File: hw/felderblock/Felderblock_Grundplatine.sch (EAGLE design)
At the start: 54 parts, among them IC2 LM2936, IC3 ULN2803, IC4 MCP2300X/P, J1 RJ11, J2 RJ11, M1 ARDUINO-NANO-3.0, T2 BC337, X1 TASTENSPERRE1, X2 TASTENSPERRE2, X3 SCHL-SPERRE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

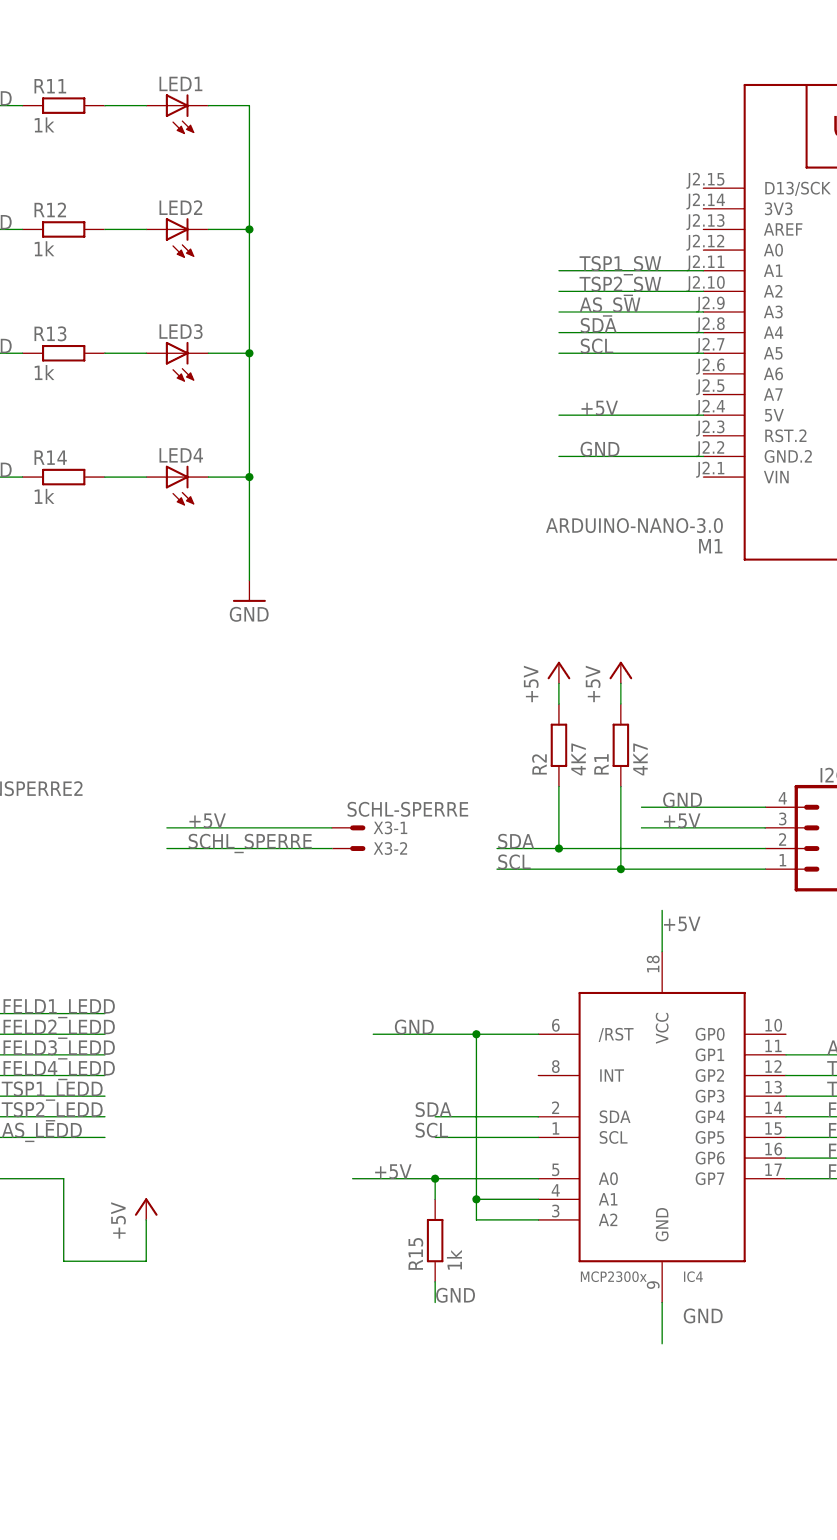
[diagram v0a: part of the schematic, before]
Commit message: corrected errors
LEDs connections corrected, address for MCP23008 corrected, reset for MCP23008 corrected
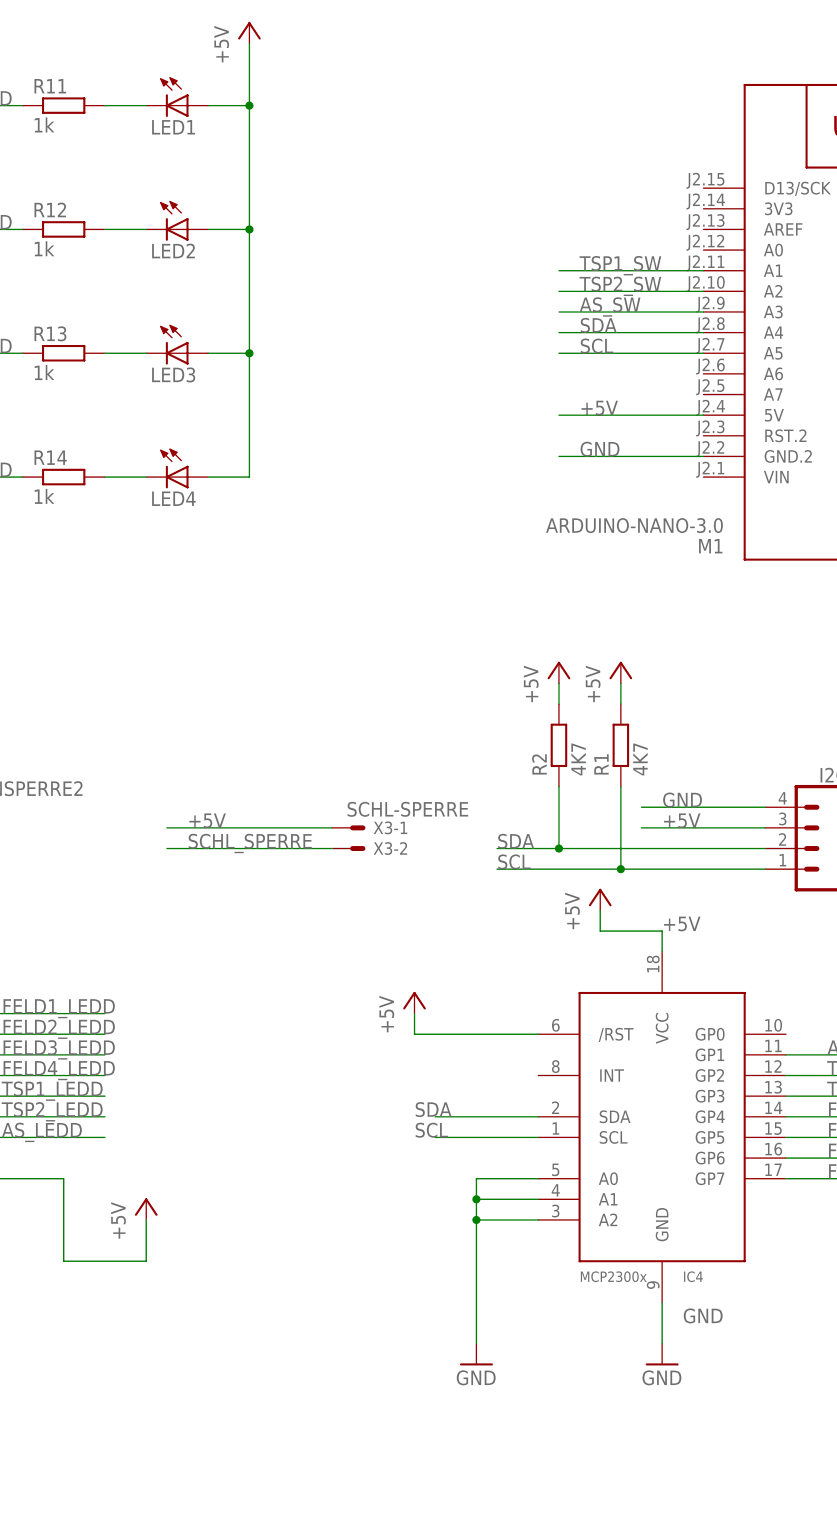
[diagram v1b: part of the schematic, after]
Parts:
- removed R15: 1k, resistor:R-EU_0207/7
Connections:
- removed net N$5: LED2.A, R12.2
- removed net N$8: LED3.A, R13.2
- removed net N$9: LED4.A, R14.2
- new net N$1: LED1.C, R11.2
- new net N$2: LED2.C, R12.2
- new net N$3: LED3.C, R13.2
- net +5V: now also IC4./RST, LED1.A, LED2.A, LED3.A, LED4.A; no longer IC4.A0, R15.2
- net GND: now also IC4.A0; no longer IC4./RST, LED1.C, LED2.C, LED3.C, LED4.C, R15.1
- net N$4: now also LED4.C, R14.2; no longer LED1.A, R11.2
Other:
- moved on the sheet: LED1, LED2, LED3, LED4

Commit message: Changed to PCA9685
- Changed LED-driver to PCA9685
- Now two LED per field
- Use LN-circuit with comparator
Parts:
- removed C2, C3: 100nF, resistor:C-EU025-025X050
- removed C6: 47pF, resistor:C-EU025-024X044
- removed C7: 1nF, resistor:C-EU025-025X050
- removed IC3: ULN2803, uln-udn:ULN2803ADIL18
- removed IC4: MCP2300X/P, adafruit:MCP2300X/P
- removed R11, R12, R13, R14: 1k, resistor:R-EU_0207/7
- added IC1: LM311N, linear:LM311N
- added LED5, LED6, LED7, LED8: (no value), led:LED3MM
- added R3: 4.7k, resistor:R-EU_0207/7
- added U$1: ADA9685-STACK, ada9685:ADA9685-STACK
- LED1, LED2, LED3, LED4: device led:LED10MM -> led:LED3MM
- R16: value 12R -> 47k
- R17: value 12R -> 150k
- R18: value 130K -> 10k
- R19: value 47k -> 22k
- R20: value 3K3 -> 220k
- X3: device con-molex:22-23-2021 -> con-molex:22-23-2041
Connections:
- removed net AS_LEDD: IC3.O7, X5-3.S
- removed net FELD1_LED: IC3.I1, IC4.GP7
- removed net FELD1_LEDD: IC3.O1, R11.1
- removed net FELD2_LED: IC3.I2, IC4.GP6
- removed net FELD2_LEDD: IC3.O2, R12.1
- removed net FELD3_LED: IC3.I3, IC4.GP5
- removed net FELD3_LEDD: IC3.O3, R13.1
- removed net FELD4_LED: IC3.I4, IC4.GP4
- removed net FELD4_LEDD: IC3.O4, R14.1
- removed net LN_INTERN: R17.2, R18.2, T2.C
- removed net N$1: LED1.C, R11.2
- removed net N$11: C6.1, R16.2, R17.1
- removed net N$2: LED2.C, R12.2
- removed net N$3: LED3.C, R13.2
- removed net N$4: LED4.C, R14.2
- removed net SCHL_SPERRE: M1.D2, X3-2.S
- removed net TSP1_LEDD: IC3.O5, X1-3.S
- removed net TSP2_LEDD: IC3.O6, X2-3.S
- new net FELD1_LED_RD: LED1.C, U$1.PWM0
- new net FELD1_LED_WS: LED5.C, U$1.PWM4
- new net FELD2_LED_RD: LED2.C, U$1.PWM1
- new net FELD2_LED_WS: LED6.C, U$1.PWM5
- new net FELD3_LED_RD: LED3.C, U$1.PWM2
- new net FELD3_LED_WS: LED7.C, U$1.PWM6
- new net FELD4_LED_RD: LED4.C, U$1.PWM3
- new net FELD4_LED_WS: LED8.C, U$1.PWM7
- new net N$5: IC1.+IN, R16.1, R17.2, R20.2
- new net N$8: IC1.-IN, R18.1, R19.2
- new net SCHL_SP_LED: U$1.PWM14, X3-3.S
- new net SCHL_SP_SW: M1.A2, X3-4.S
- net +5V: now also IC1.V+, LED5.A, LED6.A, LED7.A, LED8.A, R18.2, U$1.V+, U$1.VCC, X3-2.S; no longer C2.1, C3.1, IC3.CD+, IC4./RST, IC4.VCC, X3-1.S
- net AS_LED: now also U$1.PWM15, X5-3.S; no longer IC3.I7, IC4.GP1
- net BASE: now also R3.2; no longer C7.2, R20.2
- net GND: now also IC1.GND, IC1.V-, R17.1, U$1.GND, X3-1.S; no longer C2.2, C3.2, C6.2, IC3.GND, IC4.A0, IC4.A1, IC4.A2, IC4.GND
- net LN_RX: now also IC1.OUT, R20.1; no longer R18.1, R19.2
- net LN_TX: now also R3.1; no longer C7.1, R20.1
- net LOCONET: now also R16.2, T2.C; no longer R16.1
- net MI_FWD: now also M1.D2; no longer M1.D6
- net MI_REV: now also M1.D3; no longer M1.D5
- net SCL: now also U$1.SCL; no longer IC4.SCL
- net SDA: now also U$1.SDA; no longer IC4.SDA
- net TSP1_LED: now also U$1.PWM12, X1-3.S; no longer IC3.I5, IC4.GP3
- net TSP1_SW: now also M1.A0; no longer M1.A1
- net TSP2_LED: now also U$1.PWM13, X2-3.S; no longer IC3.I6, IC4.GP2
- net TSP2_SW: now also M1.A1; no longer M1.A2
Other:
- moved on the sheet: I2C, LED1, LED2, LED3, LED4, M1, R1, R10, R16, R17, R18, R19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

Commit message: Rearranged order of LED and switches
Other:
- moved on the sheet: U$1
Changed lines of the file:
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@@
 <?xml version="1.0" encoding="utf-8"?>
 <!DOCTYPE eagle SYSTEM "eagle.dtd">
-<eagle version="7.7.0">
+<eagle version="7.3.0">
 <drawing>
 <settings>
@@
 <grid distance="0.1" unitdist="inch" unit="inch" style="lines" multiple="1" display="no" altdistance="0.01" altunitdist="inch" altunit="inch"/>
 <layers>
-<layer number="1" name="Top" color="4" fill="1" visible="yes" active="no"/>
-<layer number="16" name="Bottom" color="1" fill="1" visible="yes" active="no"/>
-<layer number="17" name="Pads" color="2" fill="1" visible="yes" active="no"/>
-<layer number="18" name="Vias" color="2" fill="1" visible="yes" active="no"/>
-<layer number="19" name="Unrouted" color="6" fill="1" visible="yes" active="no"/>
-<layer number="20" name="Dimension" color="15" fill="1" visible="yes" active="no"/>
-<layer number="21" name="tPlace" color="7" fill="1" visible="yes" active="no"/>
-<layer number="22" name="bPlace" color="7" fill="1" visible="yes" active="no"/>
-<layer number="23" name="tOrigins" color="15" fill="1" visible="yes" active="no"/>
-<layer number="24" name="bOrigins" color="15" fill="1" visible="yes" active="no"/>
-<layer number="25" name="tNames" color="7" fill="1" visible="yes" active="no"/>
-<layer number="26" name="bNames" color="7" fill="1" visible="yes" active="no"/>
-<layer number="27" name="tValues" color="7" fill="1" visible="yes" active="no"/>
-<layer number="28" name="bValues" color="7" fill="1" visible="yes" active="no"/>
+<layer number="1" name="Top" color="4" fill="1" visible="no" active="no"/>
+<layer number="16" name="Bottom" color="1" fill="1" visible="no" active="no"/>
+<layer number="17" name="Pads" color="2" fill="1" visible="no" active="no"/>
+<layer number="18" name="Vias" color="2" fill="1" visible="no" active="no"/>
+<layer number="19" name="Unrouted" color="6" fill="1" visible="no" active="no"/>
+<layer number="20" name="Dimension" color="15" fill="1" visible="no" active="no"/>
+<layer number="21" name="tPlace" color="7" fill="1" visible="no" active="no"/>
+<layer number="22" name="bPlace" color="7" fill="1" visible="no" active="no"/>
+<layer number="23" name="tOrigins" color="15" fill="1" visible="no" active="no"/>
+<layer number="24" name="bOrigins" color="15" fill="1" visible="no" active="no"/>
+<layer number="25" name="tNames" color="7" fill="1" visible="no" active="no"/>
+<layer number="26" name="bNames" color="7" fill="1" visible="no" active="no"/>
+<layer number="27" name="tValues" color="7" fill="1" visible="no" active="no"/>
+<layer number="28" name="bValues" color="7" fill="1" visible="no" active="no"/>
 <layer number="29" name="tStop" color="7" fill="3" visible="no" active="no"/>
 <layer number="30" name="bStop" color="7" fill="6" visible="no" active="no"/>
@@
 <layer number="35" name="tGlue" color="7" fill="4" visible="no" active="no"/>
 <layer number="36" name="bGlue" color="7" fill="5" visible="no" active="no"/>
-<layer number="37" name="tTest" color="7" fill="1" visible="yes" active="no"/>
-<layer number="38" name="bTest" color="7" fill="1" visible="yes" active="no"/>
+<layer number="37" name="tTest" color="7" fill="1" visible="no" active="no"/>
+<layer number="38" name="bTest" color="7" fill="1" visible="no" active="no"/>
 <layer number="39" name="tKeepout" color="4" fill="11" visible="no" active="no"/>
 <layer number="40" name="bKeepout" color="1" fill="11" visible="no" active="no"/>
@@
 <layer number="44" name="Drills" color="7" fill="1" visible="no" active="no"/>
 <layer number="45" name="Holes" color="7" fill="1" visible="no" active="no"/>
-<layer number="46" name="Milling" color="3" fill="1" visible="yes" active="no"/>
-<layer number="47" name="Measures" color="7" fill="1" visible="yes" active="no"/>
-<layer number="48" name="Document" color="7" fill="1" visible="yes" active="no"/>
-<layer number="49" name="Reference" color="7" fill="1" visible="yes" active="no"/>
-<layer number="50" name="dxf" color="7" fill="1" visible="yes" active="no"/>
-<layer number="51" name="tDocu" color="7" fill="1" visible="yes" active="no"/>
-<layer number="52" name="bDocu" color="7" fill="1" visible="yes" active="no"/>
-<layer number="53" name="tGND_GNDA" color="7" fill="9" visible="yes" active="no"/>
-<layer number="54" name="bGND_GNDA" color="1" fill="9" visible="yes" active="no"/>
-<layer number="56" name="wert" color="7" fill="1" visible="yes" active="no"/>
-<layer number="57" name="tCAD" color="7" fill="1" visible="yes" active="no"/>
-<layer number="58" name="bCAD" color="7" fill="1" visible="yes" active="no"/>
-<layer number="59" name="tCarbon" color="7" fill="1" visible="yes" active="no"/>
-<layer number="60" name="bCarbon" color="7" fill="1" visible="yes" active="no"/>
+<layer number="46" name="Milling" color="3" fill="1" visible="no" active="no"/>
+<layer number="47" name="Measures" color="7" fill="1" visible="no" active="no"/>
+<layer number="48" name="Document" color="7" fill="1" visible="no" active="no"/>
+<layer number="49" name="Reference" color="7" fill="1" visible="no" active="no"/>
+<layer number="50" name="dxf" color="7" fill="1" visible="no" active="no"/>
+<layer number="51" name="tDocu" color="7" fill="1" visible="no" active="no"/>
+<layer number="52" name="bDocu" color="7" fill="1" visible="no" active="no"/>
+<layer number="53" name="tGND_GNDA" color="7" fill="9" visible="no" active="no"/>
+<layer number="54" name="bGND_GNDA" color="1" fill="9" visible="no" active="no"/>
+<layer number="56" name="wert" color="7" fill="1" visible="no" active="no"/>
+<layer number="57" name="tCAD" color="7" fill="1" visible="no" active="no"/>
+<layer number="58" name="bCAD" color="7" fill="1" visible="no" active="no"/>
+<layer number="59" name="tCarbon" color="7" fill="1" visible="no" active="no"/>
+<layer number="60" name="bCarbon" color="7" fill="1" visible="no" active="no"/>
 <layer number="88" name="SimResults" color="9" fill="1" visible="no" active="yes"/>
 <layer number="89" name="SimProbes" color="9" fill="1" visible="no" active="yes"/>

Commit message: Changed footprint for voltage regulator to TO220
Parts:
- IC2: value LM2936 -> MC78M05CT; device national-semiconductor:LM2936Z-5.0 -> linear:MC78M05CT
- LED1, LED2, LED3, LED4: value (none) -> Red
- LED5, LED6, LED7, LED8: value (none) -> White
- R3: value 4.7k -> 4k7
- renumbered S5 to ENCODER2, S6 to ENCODER1
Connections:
- net FELD4_LED_WS renamed FELD4_LED_WT
- removed net FELD1_LED_WS: LED5.C, U$1.PWM4
- removed net FELD2_LED_WS: LED6.C, U$1.PWM5
- removed net FELD3_LED_WS: LED7.C, U$1.PWM6
- new net FELD1_LED_WT: LED5.C, U$1.PWM1
- new net FELD2_LED_WT: LED6.C, U$1.PWM3
- new net FELD3_LED_WT: LED7.C, U$1.PWM5
- net +5V: no longer U$1.V+
- net FELD2_LED_RD: now also U$1.PWM2; no longer U$1.PWM1
- net FELD3_LED_RD: now also U$1.PWM4; no longer U$1.PWM2
- net FELD4_LED_RD: now also U$1.PWM6; no longer U$1.PWM3
- net N$7: now also IC2.VI; no longer IC2.VIN
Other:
- moved on the sheet: IC2
